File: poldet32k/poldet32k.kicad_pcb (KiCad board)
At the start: 2 copper layers, 51 x 30.7 mm, 6 parts, among them J1 GameBoy_GamePak_AGB-002, U1 AM29F040JNS

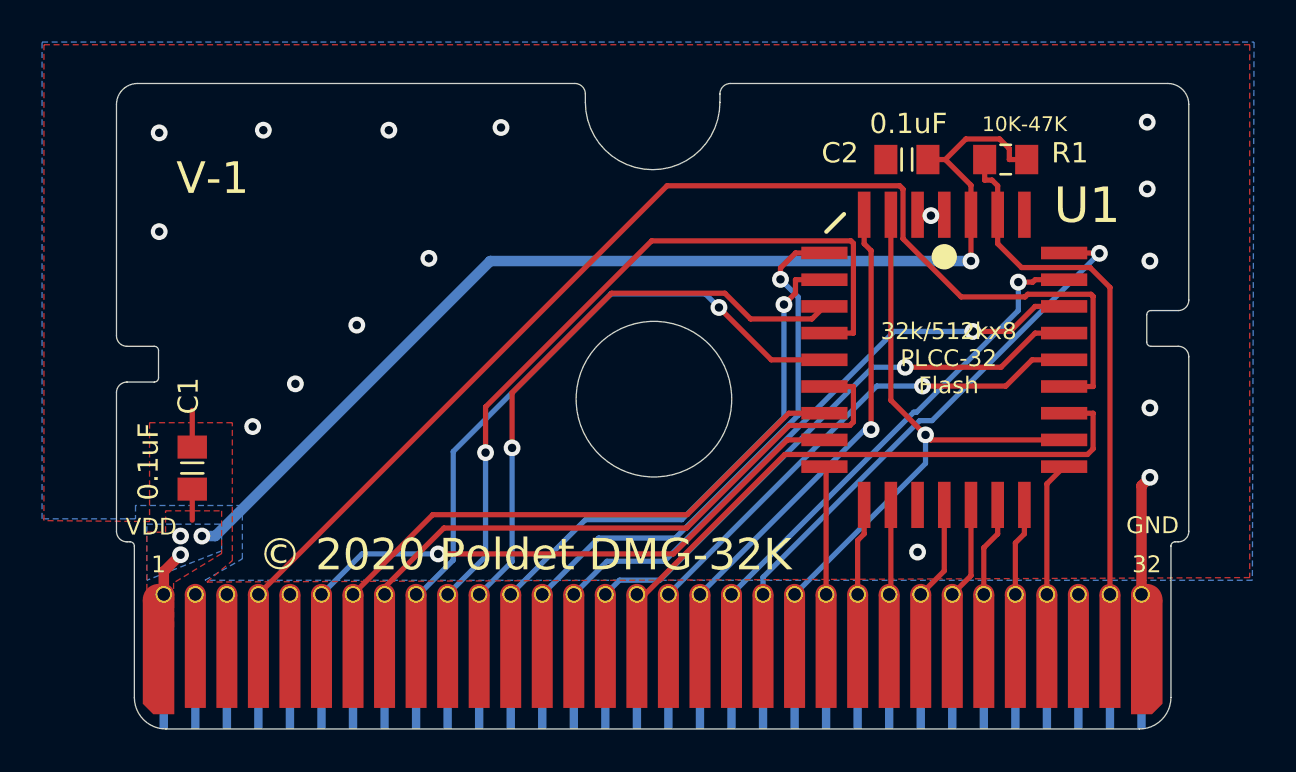
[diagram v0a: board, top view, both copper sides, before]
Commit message: Migrated some files to KiCad 7
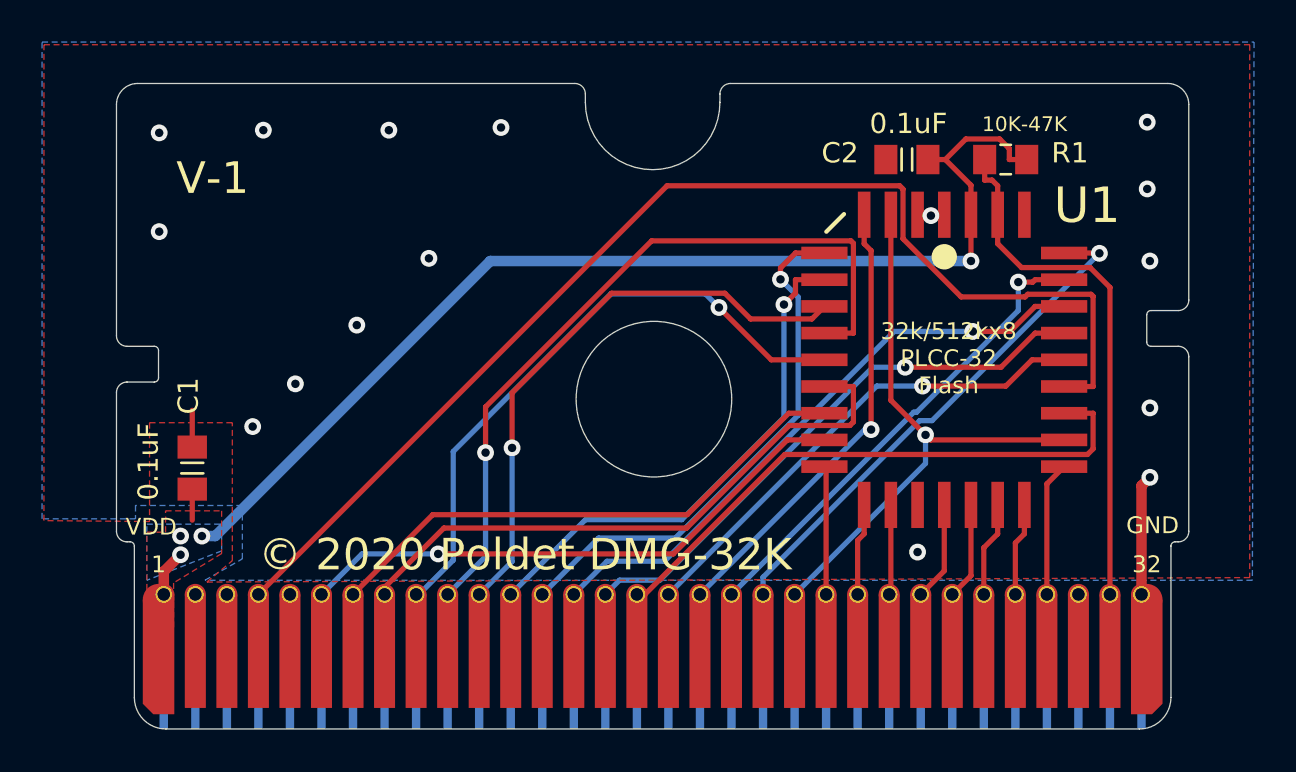
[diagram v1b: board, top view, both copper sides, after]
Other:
- net class Default removed
